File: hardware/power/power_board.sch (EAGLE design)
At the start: 72 parts, among them IC1 LM321MF, IC2 LM321MF, J1 FASTON1289_ST, J2 FASTON1289_ST, J3 12v, J4 5v, J5 XT30PW-F, J6 XT30PW-F, J7 XT30PW-F, J8 XT30PW-F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

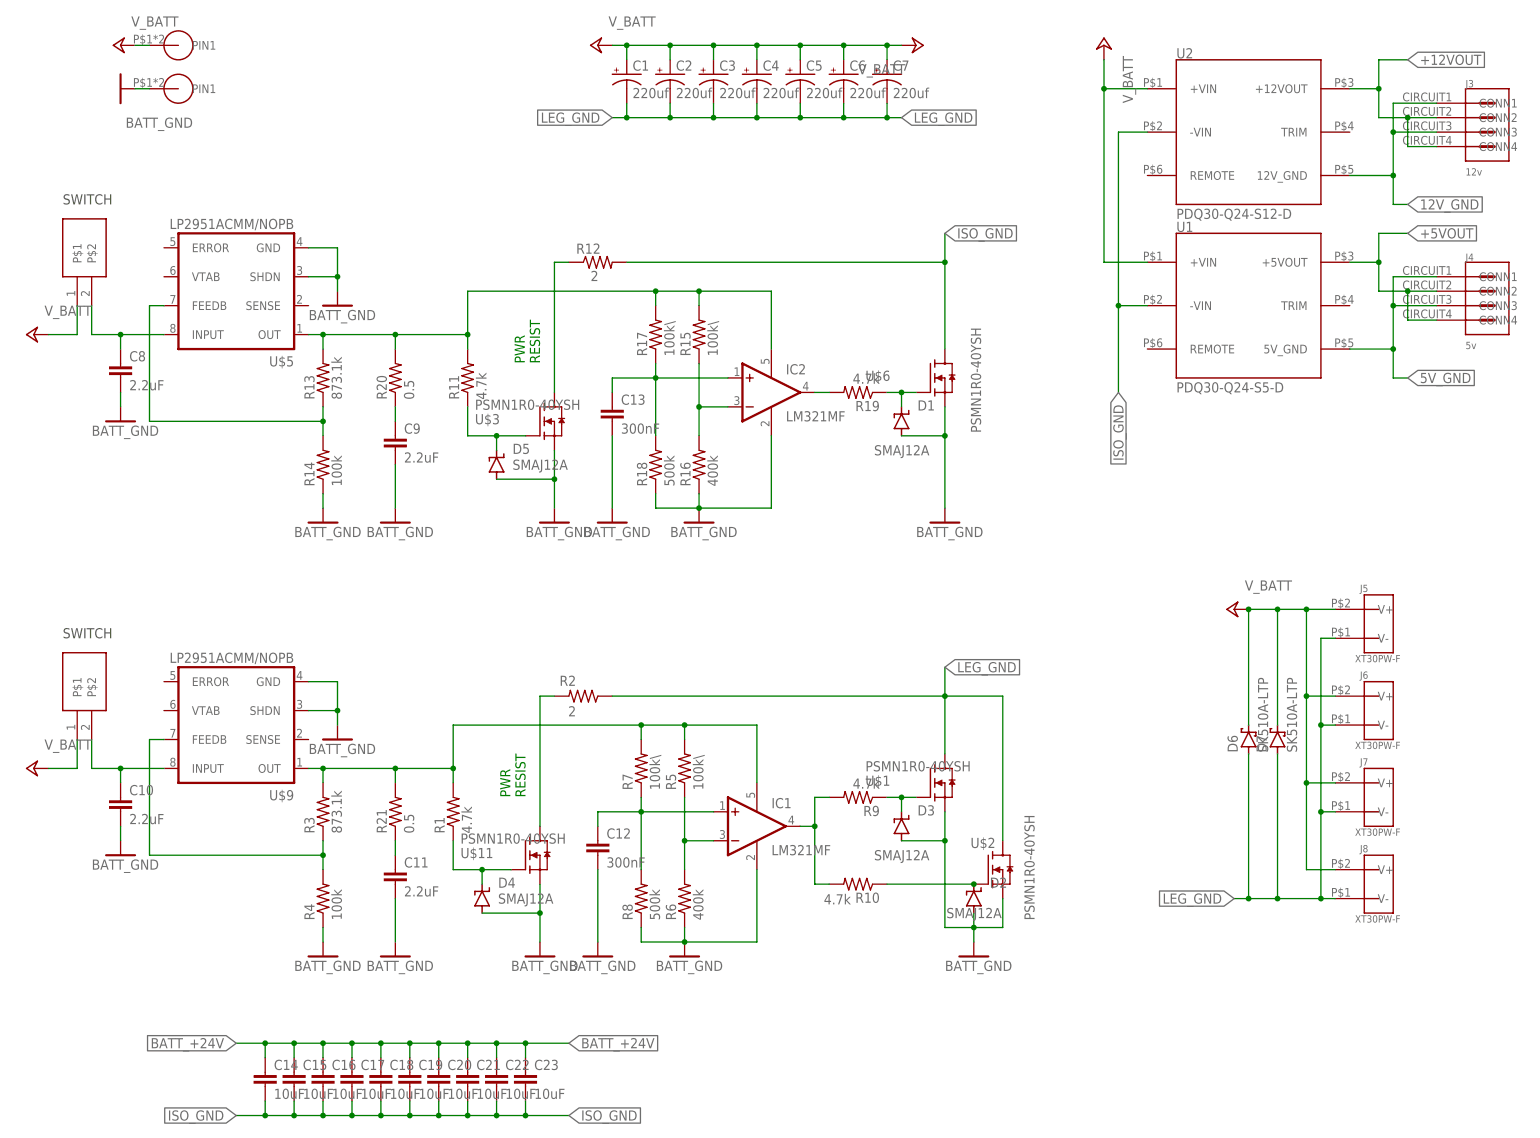
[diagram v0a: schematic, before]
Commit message: Added LEDs:
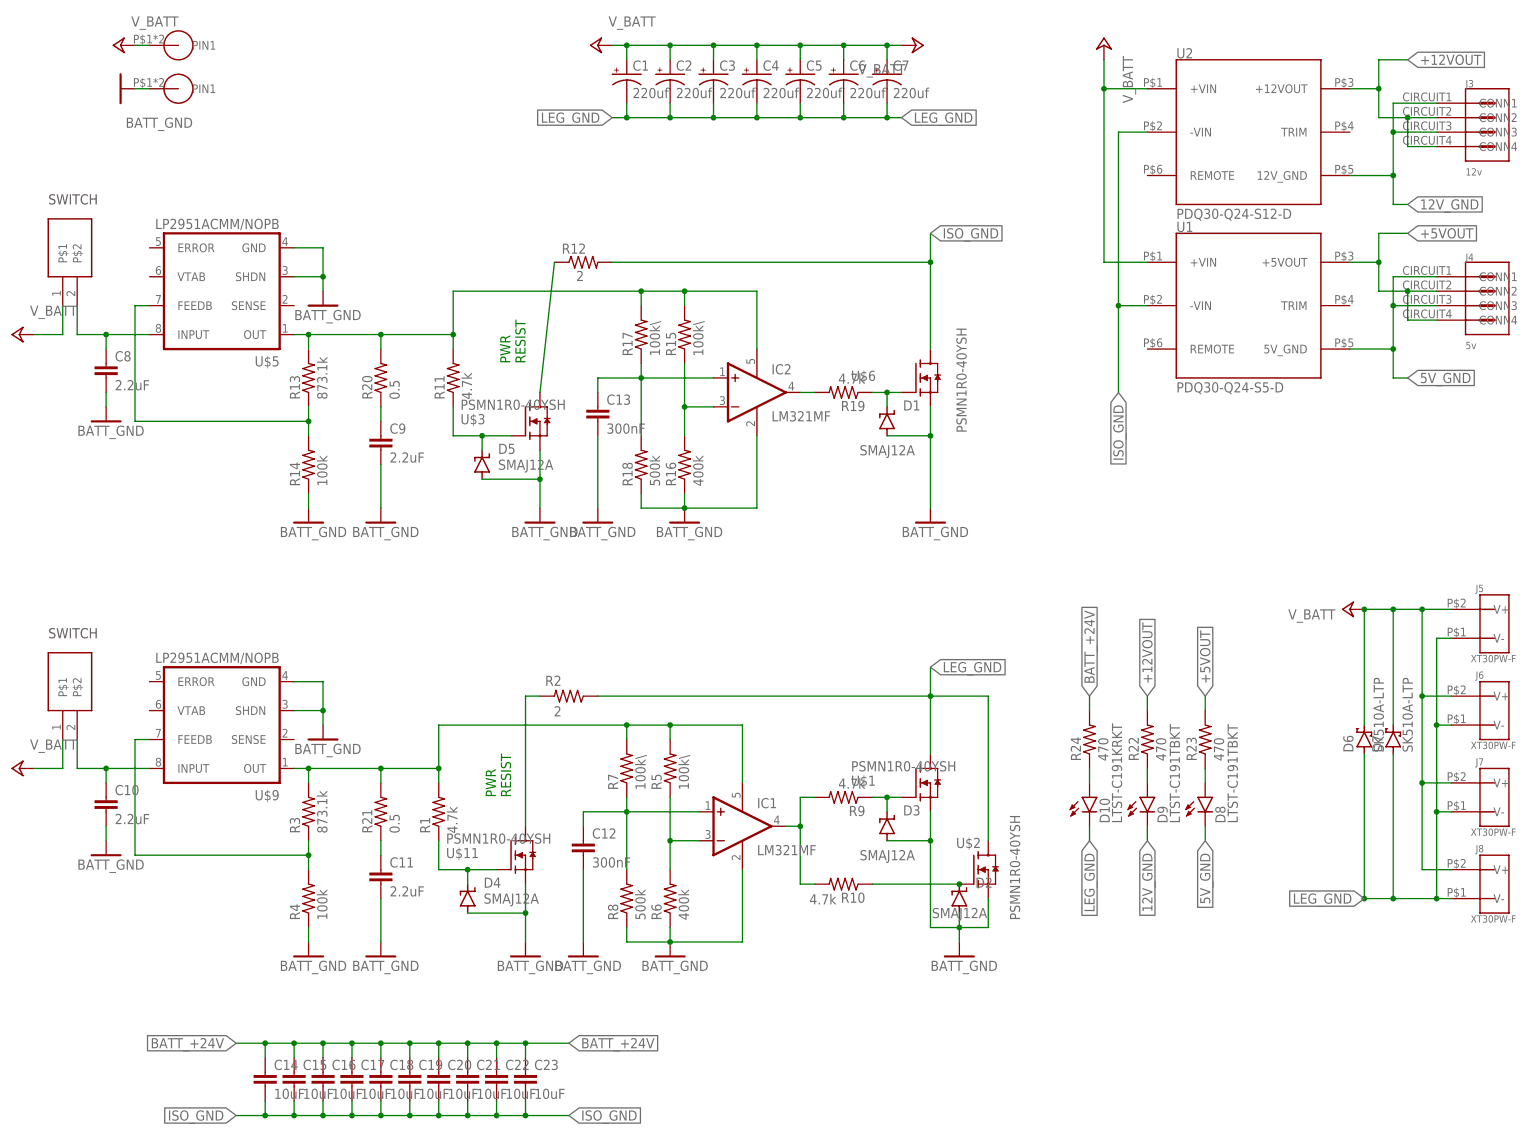
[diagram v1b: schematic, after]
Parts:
- added D10: LTST-C191KRKT, timlib:LTST-C191KRKT
- added D8, D9: LTST-C191TBKT, timlib:LTST-C191TBKT
- added R22, R23, R24: 470, rcl:R-US_R0603
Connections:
- new net N$20: D9.A, R22.1
- new net N$21: D8.A, R23.1
- new net N$22: D10.A, R24.1
- net +12VOUT: now also R22.2
- net +5VOUT: now also R23.2
- net 12V_GND: now also D9.C
- net 5V_GND: now also D8.C
- net BATT_+24V: now also R24.2
- net LEG_GND: now also D10.C
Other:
- moved on the sheet: C10, C11, C12, C13, C8, C9, D1, D2, D3, D4, D5, D6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
